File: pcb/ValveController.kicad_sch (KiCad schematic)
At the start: 87 parts, among them J10 1770966, J11 1770966, J12 1770966, J13 USB4115-03-C, J14 1990986, J15 1770885, J16 1770885, J2 1990986, J3 1990986, J8 1770966, J9 1770966, Q3 MOC3063S-TA1, Q4 MOC3063S-TA1, Q5 CSD17313Q2, Q6 CPC1017N, Q7 CPC1017N, SW1 TL9320AF400QG, U1 IRM-03-5, U2 TLV75733P, U5 ESP32-C6-WROOM-1-N4, U6 TPS61040, U7 IS31FL3730

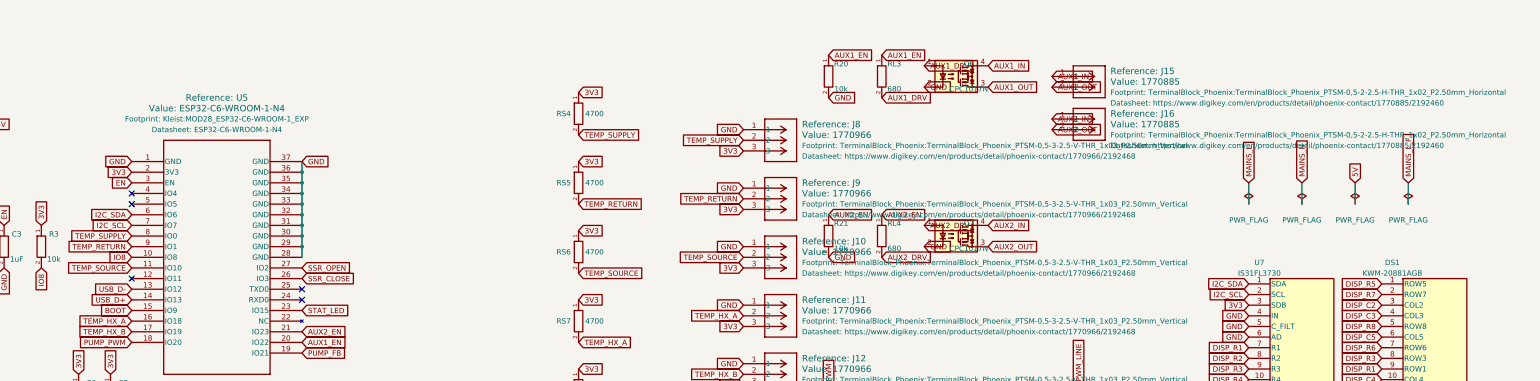
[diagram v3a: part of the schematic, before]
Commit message: feat(pcb): AC/continuity detect on AUX channels — dual AC opto + switched 24V wetting
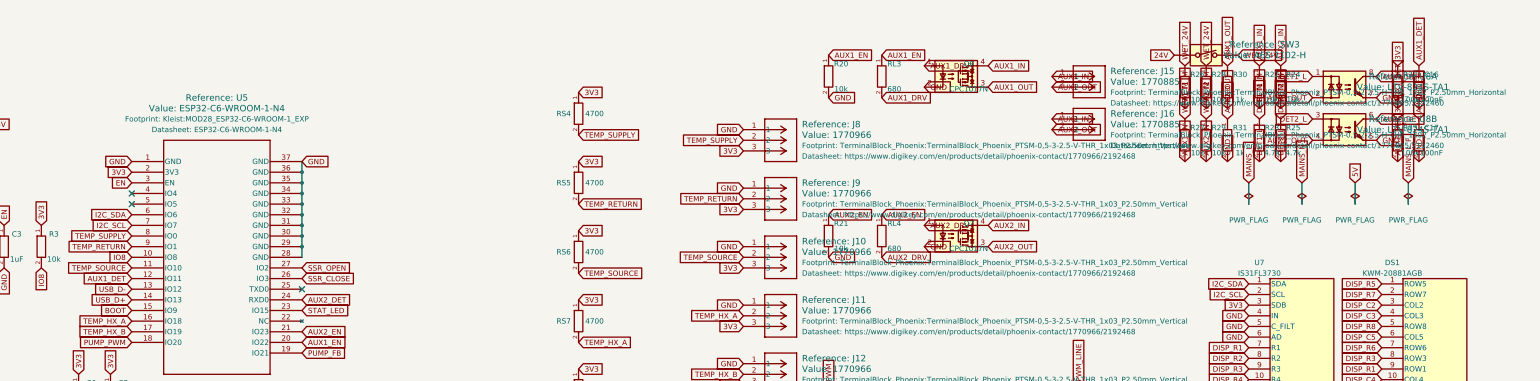
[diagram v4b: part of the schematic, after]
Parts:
- added C16, C17: 100nF, Capacitor_SMD:C_0402_1005Metric, symbol C_dev
- added R22, R24, R26, R27, R28, R29: 10k, Resistor_SMD:R_0402_1005Metric, symbol R_dev
- added R23, R25: 4.7k, Resistor_SMD:R_0402_1005Metric, symbol R_dev
- added R30, R31: 1k, Resistor_SMD:R_0402_1005Metric, symbol R_dev
- added R32, R33: 100k, Resistor_SMD:R_0402_1005Metric, symbol R_dev
- added SW3: A6S-1102-H, Button_Switch_SMD:SW_DIP_SPSTx01_Slide_Omron_A6S-110x_W8.9mm_P2.54mm, symbol Switch:SW_DIP_x01
- added U8: LTV-824S-TA1, Package_DIP:SMDIP-8_W9.53mm, symbol Isolator:LTV-824
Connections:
- net 24V: now also SW3.1
- net 3V3: now also R32.1, R33.1
- net AUX1_IN: now also R22.1, R27.2
- net AUX1_OUT: now also R30.1, U8.2
- net AUX2_IN: now also R24.1, R29.2
- net AUX2_OUT: now also R31.1, U8.4
- net GND: now also C16.2, C17.2, R30.2, R31.2, U8.5, U8.7
- net AUX1_DET: now reaches U5.12 (IO11)
- net AUX1_DET: now also C16.1, R32.2, U8.8
- net AUX2_DET: now reaches U5.24 (RXD0)
- net AUX2_DET: now also C17.1, R33.2, U8.6
- new net DET1_L: R23.2, U8.1
- new net DET1_M: R22.2, R23.1
- new net DET2_L: R25.2, U8.3
- new net DET2_M: R24.2, R25.1
- new net WET1_M: R26.2, R27.1
- new net WET2_M: R28.2, R29.1
- new net WET_24V: R26.1, R28.1, SW3.2
- no-connect marks 12 -> 10

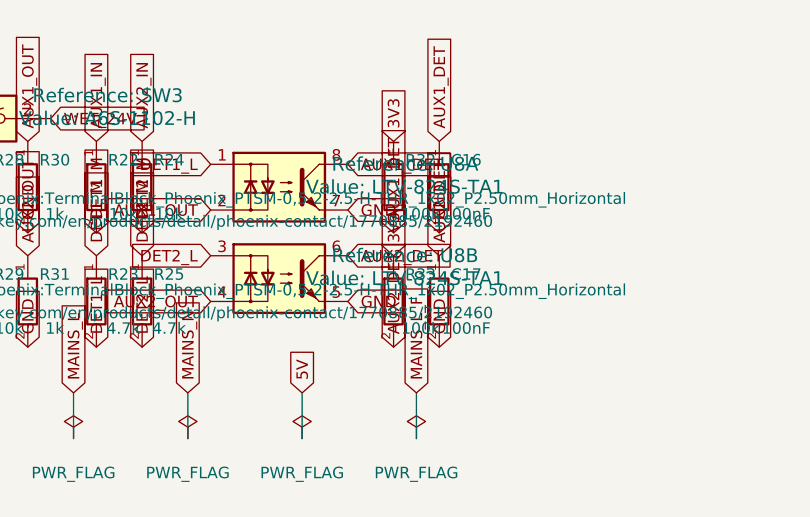
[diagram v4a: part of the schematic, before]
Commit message: fix(pcb): U8 MPN to LTV-824S — tape variant out of stock, tube in stock
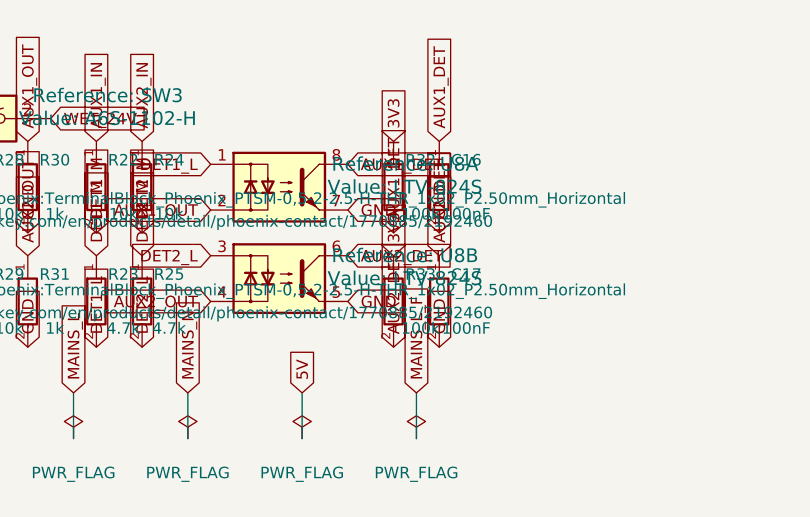
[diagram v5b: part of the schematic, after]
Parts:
- U8: value LTV-824S-TA1 -> LTV-824S; DigiKey https://www.digikey.com/en/products/detail/lite-on-inc/LTV-824S-TA1/322776 -> https://www.digikey.com/en/products/detail/lite-on-inc/LTV-824S/385817; MPN LTV-824S-TA1 -> LTV-824S
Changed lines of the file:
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@@
 			)
 		)
-		(property "Value" "LTV-824S-TA1"
+		(property "Value" "LTV-824S"
 			(at 397.51000000000005 17.78 0)
 			(show_name yes)
@@
 			)
 		)
-		(property "Datasheet" "https://www.digikey.com/en/products/detail/lite-on-inc/LTV-824S-TA1/322776"
+		(property "Datasheet" "https://www.digikey.com/en/products/detail/lite-on-inc/LTV-824S/385817"
 			(at 397.51000000000005 17.78 0)
 			(hide yes)
@@
 			)
 		)
-		(property "MPN" "LTV-824S-TA1"
+		(property "MPN" "LTV-824S"
 			(at 397.51000000000005 17.78 0)
 			(hide yes)
@@
 			)
 		)
-		(property "DigiKey" "https://www.digikey.com/en/products/detail/lite-on-inc/LTV-824S-TA1/322776"
+		(property "DigiKey" "https://www.digikey.com/en/products/detail/lite-on-inc/LTV-824S/385817"
 			(at 397.51000000000005 17.78 0)
 			(hide yes)
@@
 			)
 		)
-		(property "Value" "LTV-824S-TA1"
+		(property "Value" "LTV-824S"
 			(at 397.51000000000005 27.94 0)
 			(show_name yes)
@@
 			)
 		)
-		(property "Datasheet" "https://www.digikey.com/en/products/detail/lite-on-inc/LTV-824S-TA1/322776"
+		(property "Datasheet" "https://www.digikey.com/en/products/detail/lite-on-inc/LTV-824S/385817"
 			(at 397.51000000000005 27.94 0)
 			(hide yes)
@@
 			)
 		)
-		(property "MPN" "LTV-824S-TA1"
+		(property "MPN" "LTV-824S"
 			(at 397.51000000000005 27.94 0)
 			(hide yes)
@@
 			)
 		)
-		(property "DigiKey" "https://www.digikey.com/en/products/detail/lite-on-inc/LTV-824S-TA1/322776"
+		(property "DigiKey" "https://www.digikey.com/en/products/detail/lite-on-inc/LTV-824S/385817"
 			(at 397.51000000000005 27.94 0)
 			(hide yes)

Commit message: feat(pcb): strip status LED, USB4145 connector, reorganise schematic
The 8x8 matrix display (DS1 + U7) supersedes the D1 status LED, so D1 goes
along with R4, its GPIO15 strap pull-up — GPIO15 is Ignored with the default
eFuses, leaving it and GPIO16 as the only clean non-strapping spares.

J13 swaps from GCT USB4115 to USB4145-03-0170-C: easier to hand-solder, no
shield tabs in front of the pins. The SnapMagic-derived footprint and STEP
are gitignored — their licence permits building boards, not redistributing
model files — so regenerate with tools/import_usb4145.py. The two hand-drawn
peg keepouts are dropped; they were cut for the USB4115 body and fouled the
new 1.15 mm contact row. The abandoned UJ20 library goes with them.

Schematic reorganised into labelled functional groups: 59 footprint,
datasheet and description fields hidden (they were printing full DigiKey
URLs and library paths across the sheet), 32 field-name prefixes normalised,
30 global labels turned to read away from their own parts instead of across
them, and all 103 clusters regrouped into three bands under 10 outlines.

Netlist is byte-identical and ERC unchanged at 130 violations, category for
category, across the whole reorganisation.
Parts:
- removed D1: LED (active-low), LED_SMD:LED_0402_1005Metric, symbol C_dev
- removed R4: 1k, Resistor_SMD:R_0402_1005Metric, symbol R_dev
- J13: value USB4115-03-C -> USB4145-03-0170-C; footprint Connector_USB:USB_C_Receptacle_GCT_USB4115-03-C -> Kleist2:USB_C_Receptacle_GCT_USB4145-03-0170-C_Vertical_SMT; DigiKey https://www.digikey.nl/nl/products/detail/gct/USB4115-03-C/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 -> https://www.digikey.com/en/products/detail/gct/USB4145-03-0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; MPN USB4115-03-C -> USB4145-03-0170-C
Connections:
- net DISP_C1: now also DS1.10 (COL4); no longer DS1.13 (COL1)
- net DISP_C2: now also DS1.11 (COL6); no longer DS1.3 (COL2)
- net DISP_C3: now also DS1.13 (COL1); no longer DS1.4 (COL3)
- net DISP_C4: now also DS1.15 (COL7); no longer DS1.10 (COL4)
- net DISP_C5: now also DS1.16 (COL8); no longer DS1.6 (COL5)
- net DISP_C6: now also DS1.3 (COL2); no longer DS1.11 (COL6)
- net DISP_C7: now also DS1.4 (COL3); no longer DS1.15 (COL7)
- net DISP_C8: now also DS1.6 (COL5); no longer DS1.16 (COL8)
- net DISP_R1: now also DS1.14 (ROW2); no longer DS1.9 (ROW1)
- net DISP_R2: now also DS1.12 (ROW4); no longer DS1.14 (ROW2)
- net DISP_R3: now also DS1.9 (ROW1); no longer DS1.8 (ROW3)
- net DISP_R4: now also DS1.8 (ROW3); no longer DS1.12 (ROW4)
- net DISP_R5: now also DS1.7 (ROW6); no longer DS1.1 (ROW5)
- net DISP_R6: now also DS1.5 (ROW8); no longer DS1.7 (ROW6)
- net DISP_R8: now also DS1.1 (ROW5); no longer DS1.5 (ROW8)
- net STAT_LED: no longer names the net of U5.23 (IO15)
- no-connect marks 10 -> 11
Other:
- note added: "24V BOOST"
- note added: "8x8 MATRIX DISPLAY"
- note added: "AUX CHANNELS - 24V DRIVE & AC/CONTINUITY DETECT"
- note added: "ESP32-C6 MCU"
- note added: "MOUNTING"
- note added: "POWER - MAINS INPUT, 5V PSU, 3V3 RAIL"
- note added: "PUMP PWM & TACHO"
- note added: "TEMPERATURE SENSORS (1-Wire)"
- note added: "USB-C"
- note added: "VALVE TRIAC DRIVE (230 V)"
- moved on the sheet: C1, C10, C11, C12, C13, C14, C15, C16, C17, C2, C3, C4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

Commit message: feat: update positioning
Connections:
- net AUX1_DET: now also U8.6; no longer U8.8
- net AUX1_IN: now also J15.2; no longer J15.1
- net AUX1_OUT: now also J15.1, U8.4; no longer J15.2, U8.2
- net AUX2_DET: now also U8.8; no longer U8.6
- net AUX2_IN: now also J16.2; no longer J16.1
- net AUX2_OUT: now also J16.1, U8.2; no longer J16.2, U8.4
- net DET1_L: now also U8.3; no longer U8.1
- net DET2_L: now also U8.1; no longer U8.3
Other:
- moved on the sheet: J15, J16
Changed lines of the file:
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@@
 	(global_label "GND"
 		(shape input)
-		(at 308.61 58.42 0)
+		(at 308.61 26.67 0)
 		(effects
 			(font
@@
 		)
 		(property "Intersheetrefs" "${INTERSHEET_REFS}"
-			(at 308.61 58.42 0)
+			(at 308.61 26.67 0)
 			(hide yes)
 			(show_name no)
@@
 	(global_label "AUX2_OUT"
 		(shape input)
-		(at 205.74 49.53 0)
+		(at 205.74 54.61 180)
 		(effects
 			(font
 				(size 1.27 1.27)
 			)
-			(justify left)
+			(justify right)
 		)
 		(property "Intersheetrefs" "${INTERSHEET_REFS}"
-			(at 205.74 49.53 0)
+			(at 205.74 54.61 0)
 			(hide yes)
 			(show_name no)
@@
 	(global_label "GND"
 		(shape input)
-		(at 308.61 26.67 0)
+		(at 308.61 58.42 0)
 		(effects
 			(font
@@
 		)
 		(property "Intersheetrefs" "${INTERSHEET_REFS}"
-			(at 308.61 26.67 0)
+			(at 308.61 58.42 0)
 			(hide yes)
 			(show_name no)
@@
 	(global_label "AUX2_OUT"
 		(shape input)
-		(at 293.37 58.42 180)
+		(at 293.37 26.67 180)
 		(effects
 			(font
@@
 		)
 		(property "Intersheetrefs" "${INTERSHEET_REFS}"
-			(at 293.37 58.42 0)
+			(at 293.37 26.67 0)
 			(hide yes)
 			(show_name no)
@@
 	(global_label "AUX1_IN"
 		(shape input)
-		(at 205.74 36.83 0)
+		(at 205.74 46.99 180)
 		(effects
 			(font
 				(size 1.27 1.27)
 			)
-			(justify left)
+			(justify right)
 		)
 		(property "Intersheetrefs" "${INTERSHEET_REFS}"
-			(at 205.74 36.83 0)
+			(at 205.74 46.99 0)
 			(hide yes)
 			(show_name no)
@@
 	(global_label "AUX1_OUT"
 		(shape input)
-		(at 293.37 26.67 180)
+		(at 293.37 58.42 180)
 		(effects
 			(font
@@
 		)
 		(property "Intersheetrefs" "${INTERSHEET_REFS}"
-			(at 293.37 26.67 0)
+			(at 293.37 58.42 0)
 			(hide yes)
 			(show_name no)
@@
 	(global_label "DET2_L"
 		(shape input)
-		(at 293.37 53.34 180)
+		(at 293.37 21.59 180)
 		(effects
 			(font
@@
 		)
 		(property "Intersheetrefs" "${INTERSHEET_REFS}"
-			(at 293.37 53.34 0)
+			(at 293.37 21.59 0)
 			(hide yes)
 			(show_name no)
@@
 	(global_label "DET1_L"
 		(shape input)
-		(at 293.37 21.59 180)
+		(at 293.37 53.34 180)
 		(effects
 			(font
@@
 		)
 		(property "Intersheetrefs" "${INTERSHEET_REFS}"
-			(at 293.37 21.59 0)
+			(at 293.37 53.34 0)
 			(hide yes)
 			(show_name no)
@@
 	(global_label "AUX2_DET"
 		(shape input)
-		(at 308.61 53.34 0)
+		(at 308.61 21.59 0)
 		(effects
 			(font
@@
 		)
 		(property "Intersheetrefs" "${INTERSHEET_REFS}"
-			(at 308.61 53.34 0)
+			(at 308.61 21.59 0)
 			(hide yes)
 			(show_name no)
@@
 	(global_label "AUX1_DET"
 		(shape input)
-		(at 308.61 21.59 0)
+		(at 308.61 53.34 0)
 		(effects
 			(font
@@
 		)
 		(property "Intersheetrefs" "${INTERSHEET_REFS}"
-			(at 308.61 21.59 0)
+			(at 308.61 53.34 0)
 			(hide yes)
 			(show_name no)
@@
 	(global_label "AUX1_OUT"
 		(shape input)
-		(at 205.74 39.37 0)
+		(at 205.74 44.45 180)
 		(effects
 			(font
 				(size 1.27 1.27)
 			)
-			(justify left)
+			(justify right)
 		)
 		(property "Intersheetrefs" "${INTERSHEET_REFS}"
-			(at 205.74 39.37 0)
+			(at 205.74 44.45 0)
 			(hide yes)
 			(show_name no)
@@
 	(global_label "AUX2_IN"
 		(shape input)
-		(at 205.74 46.99 0)
+		(at 205.74 57.15 180)
 		(effects
 			(font
 				(size 1.27 1.27)
 			)
-			(justify left)
+			(justify right)
 		)
 		(property "Intersheetrefs" "${INTERSHEET_REFS}"
-			(at 205.74 46.99 0)
+			(at 205.74 57.15 0)
 			(hide yes)
 			(show_name no)
@@
 	(symbol
 		(lib_id "Kleist:1770885")
-		(at 205.74 46.99 0)
+		(at 205.74 54.61 0)
 		(unit 1)
 		(body_style 1)
@@
 		(fields_autoplaced yes)
 		(property "Reference" "J16"
-			(at 219.71 45.72 0)
+			(at 219.71 53.34 0)
 			(show_name no)
 			(do_not_autoplace no)
@@
 		)
 		(property "Value" "1770885"
-			(at 220.98 48.26 0)
+			(at 220.98 55.88 0)
 			(show_name no)
 			(do_not_autoplace no)
@@
 		)
 		(property "Footprint" "TerminalBlock_Phoenix:TerminalBlock_Phoenix_PTSM-0,5-2-2.5-H-THR_1x02_P2.50mm_Horizontal"
-			(at 219.71 50.8 0)
+			(at 219.71 58.42 0)
 			(hide yes)
 			(show_name no)
@@
 		)
 		(property "Datasheet" "https://www.digikey.com/en/products/detail/phoenix-contact/1770885/2192460"
-			(at 219.71 53.34 0)
+			(at 219.71 60.96 0)
 			(hide yes)
 			(show_name no)
@@
 		)
 		(property "Description" ""
-			(at 205.74 46.99 0)
+			(at 205.74 54.61 0)
 			(hide yes)
 			(show_name no)
@@
 		)
 		(property "MPN" "1770885"
-			(at 205.74 46.99 0)
+			(at 205.74 54.61 0)
 			(hide yes)
 			(show_name no)
@@
 		)
 		(property "DigiKey" "https://www.digikey.com/en/products/detail/phoenix-contact/1770885/2192460"
-			(at 205.74 46.99 0)
+			(at 205.74 54.61 0)
 			(hide yes)
 			(show_name no)
@@
 	(symbol
 		(lib_id "Kleist:1770885")
-		(at 205.74 36.83 0)
+		(at 205.74 44.45 0)
 		(unit 1)
 		(body_style 1)
@@
 		(fields_autoplaced yes)
 		(property "Reference" "J15"
-			(at 219.71 35.56 0)
+			(at 219.71 43.18 0)
 			(show_name no)
 			(do_not_autoplace no)
@@
 		)
 		(property "Value" "1770885"
-			(at 220.98 38.1 0)
+			(at 220.98 45.72 0)
 			(show_name no)
 			(do_not_autoplace no)
@@
 		)
 		(property "Footprint" "TerminalBlock_Phoenix:TerminalBlock_Phoenix_PTSM-0,5-2-2.5-H-THR_1x02_P2.50mm_Horizontal"
-			(at 219.71 40.64 0)
+			(at 219.71 48.26 0)
 			(hide yes)
 			(show_name no)
@@
 		)
 		(property "Datasheet" "https://www.digikey.com/en/products/detail/phoenix-contact/1770885/2192460"
-			(at 219.71 43.18 0)
+			(at 219.71 50.8 0)
 			(hide yes)
 			(show_name no)
@@
 		)
 		(property "Description" ""
-			(at 205.74 36.83 0)
+			(at 205.74 44.45 0)
 			(hide yes)
 			(show_name no)
@@
 		)
 		(property "MPN" "1770885"
-			(at 205.74 36.83 0)
+			(at 205.74 44.45 0)
 			(hide yes)
 			(show_name no)
@@
 		)
 		(property "DigiKey" "https://www.digikey.com/en/products/detail/phoenix-contact/1770885/2192460"
-			(at 205.74 36.83 0)
+			(at 205.74 44.45 0)
 			(hide yes)
 			(show_name no)
